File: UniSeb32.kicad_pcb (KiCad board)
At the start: 4 copper layers, 72 x 100 mm, 60 parts, among them J1 IO, J2 ARJM11C7-114-BA-EW2, J3 Conn_02x05_Odd_Even, J6 SDS011, J7 Conn_01x02_Female, J8 Conn_01x02_Female, U1 mini_esp32, U2 LAN8720A, U3 AMS1117-3.3, U4 AMS5919, U5 module_bme280, U6 RT9400, U7 MCP23008-xSS, U8 HLK-PM01, X1 233-508, X2 233-503, X3 233-504, Y1 Crystal_GND23

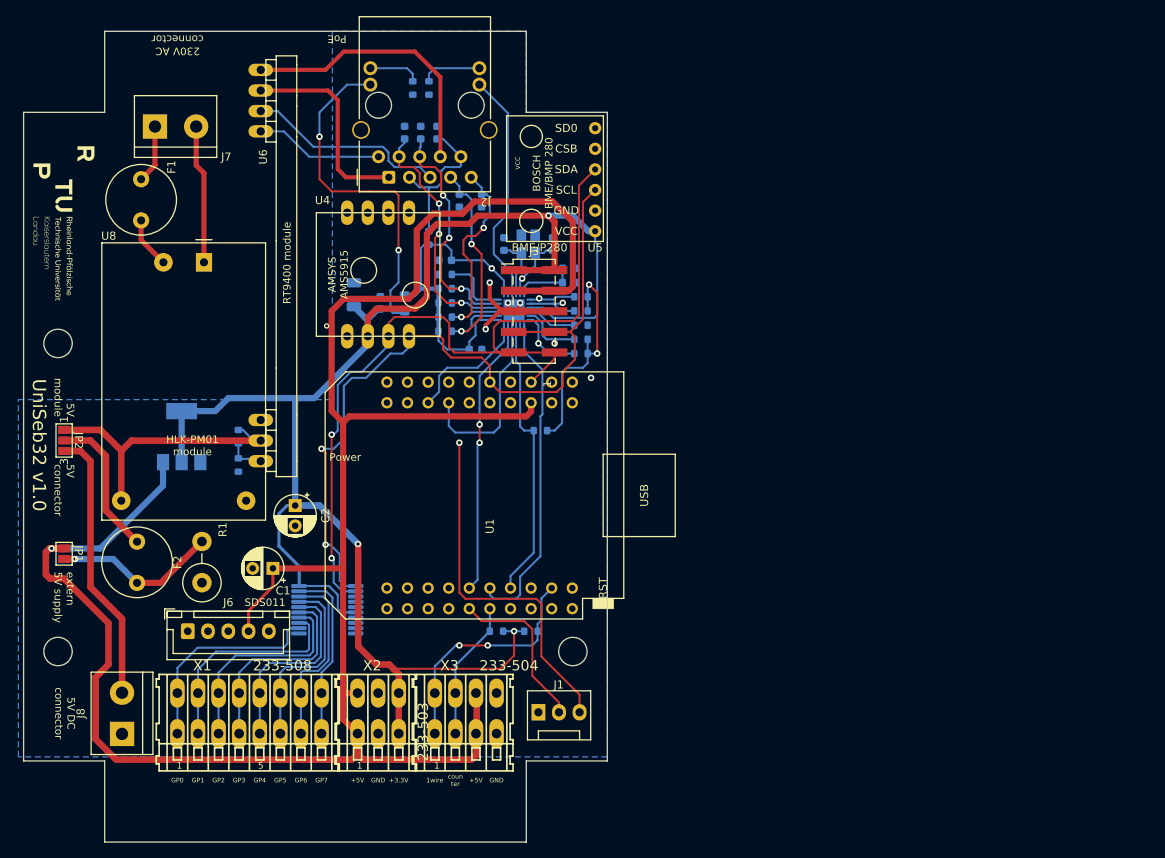
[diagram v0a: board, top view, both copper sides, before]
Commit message: Added attributes for jlcpcb assembly
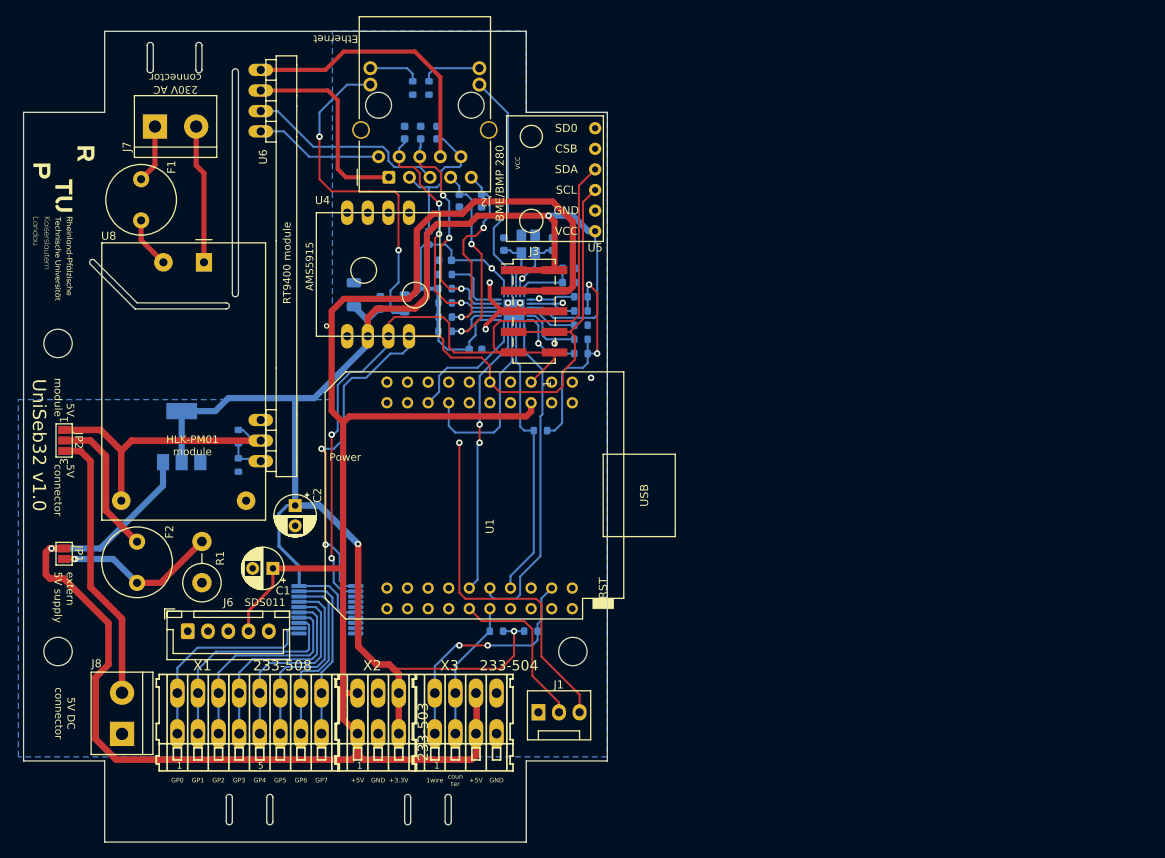
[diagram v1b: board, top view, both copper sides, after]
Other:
- outline, holes or cut-outs redrawn
- board text added: "AMS5915"
- board text added: "Ethernet"
- board text removed: "AMSYS AMS5915"
- board text removed: "BOSCH BME/BMP 280"
- board text removed: "PoE"

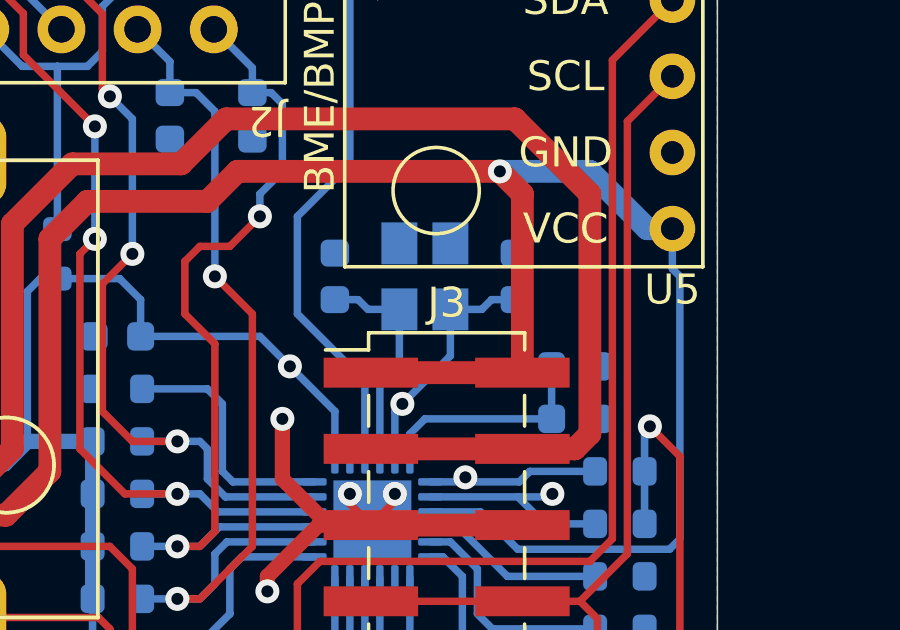
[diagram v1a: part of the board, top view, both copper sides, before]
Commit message: Fixes wrong pin numbering at Y1
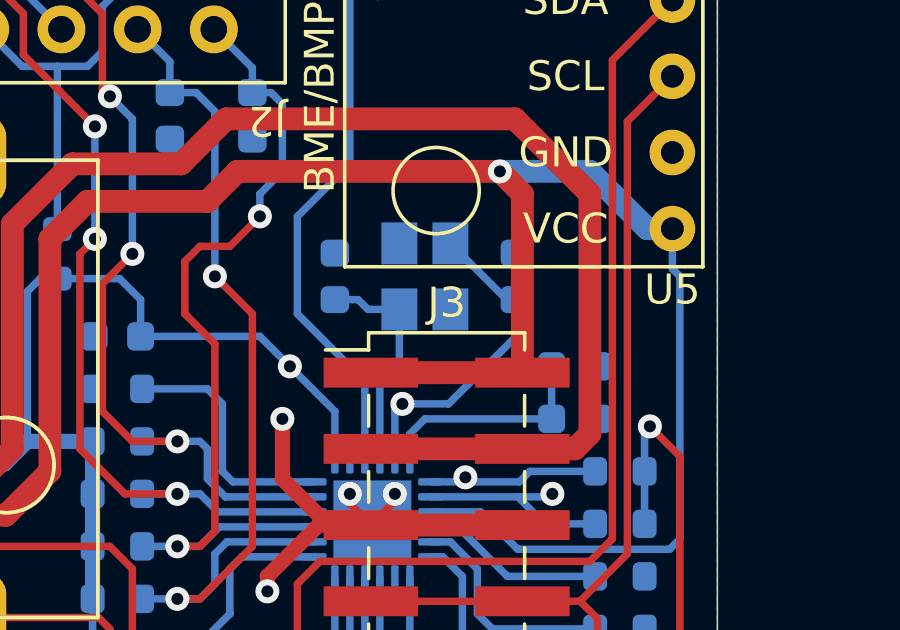
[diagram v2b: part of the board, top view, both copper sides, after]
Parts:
- Y1: value Crystal_GND23 -> 25 MHz
- turned Y1 to -90 degrees
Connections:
- Y1 pad 1: Net-(C14-Pad1) -> /IO17_RCLK
- Y1 pad 3: GND -> Net-(C14-Pad1)
- Y1 pad 4: /IO17_RCLK -> GND
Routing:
- net /IO17_RCLK: track 26.1 -> 28.9 mm

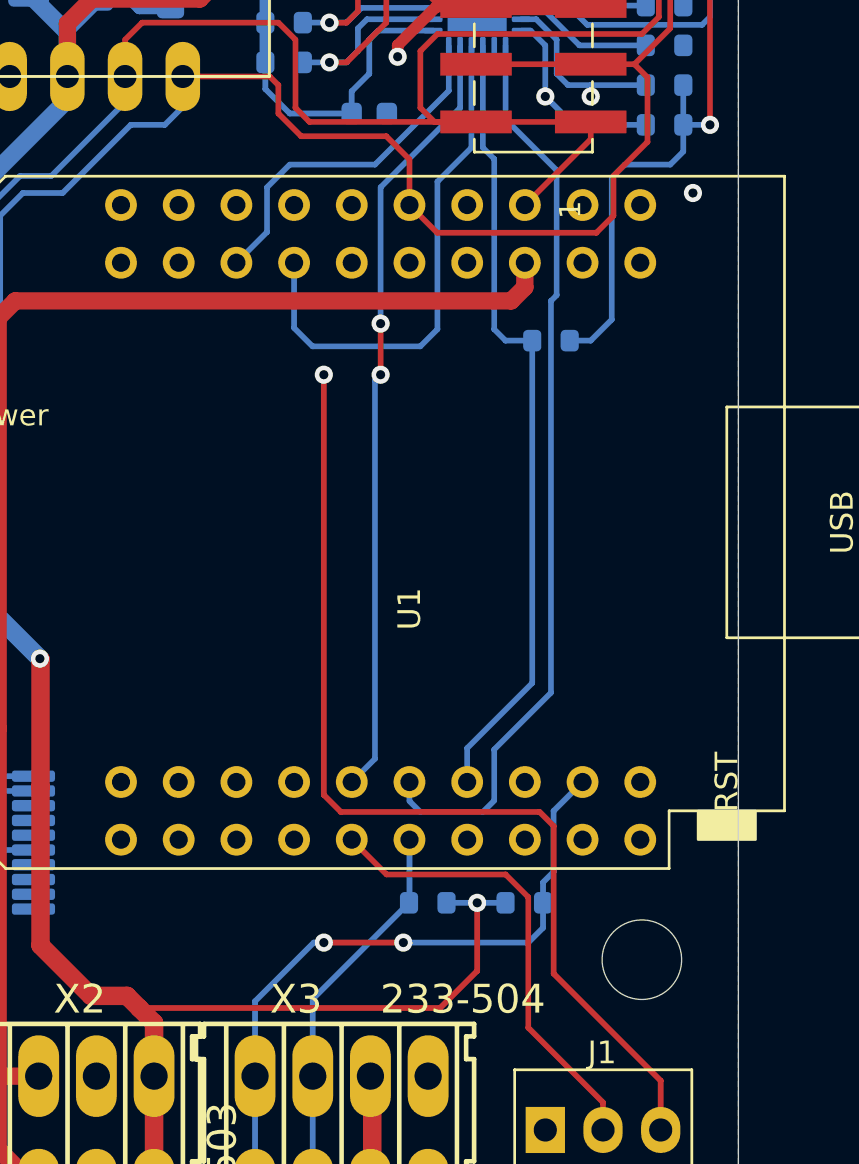
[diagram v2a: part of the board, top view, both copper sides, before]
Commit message: corrected mapping of pins added SD slot removed crystal y1 and capacitors in bom and cpl file
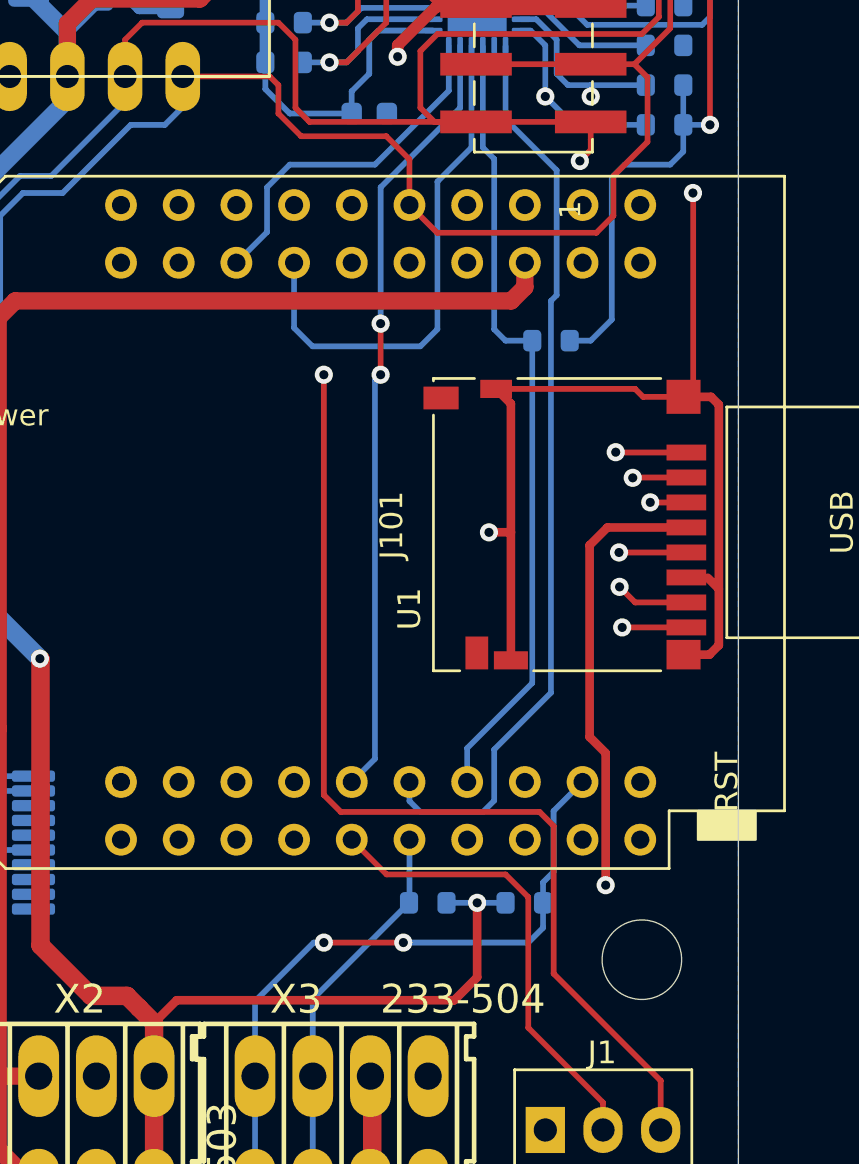
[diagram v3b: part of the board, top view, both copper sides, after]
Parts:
- added J101: Micro_SD_Card_Det, Connector_Card:microSD_HC_Hirose_DM3D-SF, F.Cu at (176.9, 112.3)
- U4: value AMS5919 -> AMS5915
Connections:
- U1 pad 13: /SDS_RX -> /SDS_TX
- U1 pad 17: unconnected-(U1-Pad17) -> /SD2
- U1 pad 19: unconnected-(U1-Pad19) -> /SCMD
- U1 pad 20: unconnected-(U1-Pad20) -> /SD3
- U1 pad 30: /SDS_TX -> /SDS_RX
- U1 pad 31: unconnected-(U1-Pad31) -> /SDA
- U1 pad 36: /SDA -> unconnected-(U1-Pad36)
- U1 pad 38: unconnected-(U1-Pad38) -> /SD1
- U1 pad 39: unconnected-(U1-Pad39) -> /SD0
- U1 pad 40: unconnected-(U1-Pad40) -> /SCLK
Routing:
- net GND: track 36.4 -> 81.9 mm, vias 5 -> 6
- net +3.3V: track 249.0 -> 274.8 mm, vias 5 -> 6
- net /SD1: track 0.00 -> 24.0 mm, vias 0 -> 1
- net /SD2: track 0.00 -> 21.7 mm, vias 0 -> 1
- net /SCLK: track 0.00 -> 20.9 mm, vias 0 -> 1
- net /SD0: track 0.00 -> 19.5 mm, vias 0 -> 1
- net /SCMD: track 0.00 -> 17.5 mm, vias 0 -> 1
- net /SD3: track 0.00 -> 16.6 mm, vias 0 -> 1
- net /SDS_RX: track 41.6 -> 53.0 mm
- net /SDS_TX: track 54.6 -> 43.8 mm
- net /SDA: track 103.5 -> 111.3 mm, vias 2 -> 3

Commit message: .
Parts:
- removed R2: 0, Resistor_SMD:R_0603_1608Metric
- moved C9 34.6 mm to (158.6, 117.3), turned to -90 degrees
- moved C13 29.0 mm to (171.5, 113.3), turned to 0 degrees
- moved C14 26.7 mm to (160.8, 105.7)
- moved C15 26.7 mm to (166.8, 105.7)
- moved Y1 26.7 mm to (163.8, 105.7)
- moved R15 25.7 mm to (171.5, 115.0)
- moved R17 25.7 mm to (171.5, 118.5)
- moved R18 25.7 mm to (171.5, 116.8)
- moved U2 25.3 mm to (163.6, 112.8)
- moved R10 25.3 mm to (155.1, 115.5)
- moved R11 25.3 mm to (155.1, 110.2)
- moved R13 25.3 mm to (155.1, 112.0)
- moved R9 25.3 mm to (155.1, 113.7)
- moved C10 24.4 mm to (160.5, 117.3), turned to -90 degrees
- moved R19 24.0 mm to (171.5, 109.7)
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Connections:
- C4 pad 2: Net-(C4-Pad2) -> 3V3-2
- J1 pad 2: /IO33 -> /IO35
- J1 pad 3: /IO32 -> /IO33
- J2 pad 4: Net-(C4-Pad2) -> 3V3-2
- J2 pad 9: Net-(C4-Pad2) -> 3V3-2
- U1 pad 28: /IO32 -> unconnected-(U1-Pad28)
- U1 pad 7: unconnected-(U1-Pad7) -> /IO35
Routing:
- net /EMAC_RXD1: track 59.0 -> 0.00 mm, vias 1 -> 0
- net GND: track 81.9 -> 24.5 mm, vias 6 -> 8
- net /IO32: track 52.5 -> 0.00 mm, vias 1 -> 0
- net /EMAC_MDI0: track 49.7 -> 0.00 mm, vias 1 -> 0
- net 3V3-2: track 82.7 -> 40.9 mm, vias 3 -> 0
- net /EMAC_MDC: track 40.3 -> 0.00 mm
- net /EMAC_RXD0: track 37.2 -> 0.00 mm, vias 1 -> 0
- net /IO5_RST: track 35.2 -> 0.00 mm
- net /EMAC_TXD0: track 34.4 -> 0.00 mm, vias 2 -> 0
- net Net-(C6-Pad1): track 29.7 -> 0.00 mm, vias 2 -> 0
- net Net-(C8-Pad1): track 32.1 -> 2.48 mm, vias 3 -> 0
- net /IO17_RCLK: track 28.9 -> 0.00 mm, vias 1 -> 0
- net /EMAC_CRS_DV: track 28.9 -> 0.00 mm, vias 1 -> 0
- net Net-(C7-Pad2): track 30.3 -> 2.25 mm, vias 3 -> 0
- net Net-(C5-Pad1): track 27.9 -> 0.00 mm, vias 2 -> 0
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- added copper zone on F.Cu, net GND

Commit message: .
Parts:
- removed C15: 30p, Capacitor_SMD:C_0603_1608Metric
- removed REF** (x3): MountingHole_3.5mm, MountingHole:MountingHole_3.5mm
- removed Y1: 25 MHz, Crystal:Crystal_SMD_3225-4Pin_3.2x2.5mm
- added JP3: SolderJumper_2_Open, Jumper:SolderJumper-2_P1.3mm_Open_Pad1.0x1.5mm, B.Cu at (148.0, 102.8)
- C14: value 30p -> 1n
- C9: value 10uf -> 10u
- moved U4 80.6 mm to (223.2, 129.8)
- moved U5 80.6 mm to (244.9, 112.0)
- moved J3 80.6 mm to (242.5, 134.3)
- moved C14 39.1 mm to (172.2, 68.2), turned to -90 degrees
- moved C3 17.6 mm to (151.2, 105.0), turned to -90 degrees
- moved L1 16.9 mm to (154.5, 104.8)
- moved R11 16.2 mm to (157.5, 94.2), turned to -90 degrees
- moved R9 15.7 mm to (155.5, 98.0), turned to -90 degrees
- moved R16 15.7 mm to (165.5, 103.2)
- moved C10 14.8 mm to (160.2, 102.5)
- moved C9 14.8 mm to (158.3, 102.5)
- moved C13 14.8 mm to (171.8, 98.5)
- moved J101 14.8 mm to (177.1, 97.6)
- moved R15 14.8 mm to (171.8, 100.3)
- moved R17 14.8 mm to (171.8, 103.8)
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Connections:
- C14 pad 1: Net-(C14-Pad1) -> Net-(J2-PadSH)
- J2 pad 11: +3.3V -> 3V3-2
- J2 pad SH: GND -> Net-(J2-PadSH)
- U2 pad 4: Net-(C14-Pad1) -> unconnected-(U2-Pad4)
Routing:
- net +3.3V: track 249.1 -> 132.6 mm, vias 6 -> 3
- net +5V: track 263.4 -> 149.9 mm
- net /SDA: track 111.3 -> 6.26 mm, vias 2 -> 1
- net /SCL: track 98.2 -> 7.73 mm, vias 2 -> 1
- net Net-(C6-Pad1): track 0.00 -> 61.2 mm, vias 0 -> 2
- net Net-(C5-Pad1): track 0.00 -> 58.3 mm, vias 0 -> 2
- net Net-(C7-Pad2): track 2.25 -> 56.0 mm
- net Net-(C8-Pad1): track 2.48 -> 56.3 mm
- net /EMAC_CRS_DV: track 0.00 -> 28.9 mm, vias 0 -> 1
- net /EMAC_RXD0: track 0.00 -> 27.8 mm, vias 0 -> 1
- net /SDS_RX: track 60.1 -> 35.8 mm
- net /EMAC_TX_EN: track 0.00 -> 24.2 mm, vias 0 -> 1
- net /EMAC_RXD1: track 0.00 -> 24.1 mm, vias 0 -> 1
- net GND: track 24.5 -> 0.62 mm, vias 8 -> 6
- net Net-(J2-Pad13): track 19.8 -> 42.1 mm
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
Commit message: .
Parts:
- added C15: 1n, Capacitor_SMD:C_0603_1608Metric, B.Cu at (171.0, 64.2)
- moved J3 94.6 mm to (148.2, 126.5)
- moved U5 67.4 mm to (177.7, 115.5)
- moved U4 62.3 mm to (161.2, 123.2)
- moved C14 19.7 mm to (153.0, 64.2), turned to 90 degrees
- moved C6 8.25 mm to (164.0, 67.5), turned to 90 degrees
- moved C5 7.27 mm to (167.5, 67.5), turned to 90 degrees
- moved C4 5.03 mm to (165.8, 67.5), turned to -90 degrees
- moved C1 3.12 mm to (141.4, 118.8)
- moved J6 2.02 mm to (130.8, 128.7)
- moved U6 1.30 mm to (143.8, 82.5)
- moved C3 1.25 mm to (151.2, 103.8)
- moved R1 0.87 mm to (134.0, 122.3)
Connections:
- net Net-(C5-Pad1) renamed /TX_P
- net Net-(C6-Pad1) renamed /TX_N
- net Net-(C7-Pad2) renamed /RX_P
- net Net-(C8-Pad1) renamed /RX_N
- C14 pad 1: Net-(J2-PadSH) -> Net-(J2-PadSH2)
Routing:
- net 3V3-2: track 32.3 -> 122.3 mm, vias 0 -> 8
- net /SDS_TX: track 41.3 -> 0.00 mm
- net /SDS_RX: track 35.8 -> 0.00 mm
- net +3.3V: track 132.6 -> 167.4 mm, vias 3 -> 5
- net +5V: track 149.9 -> 116.9 mm
- net /EMAC_TXD0: track 12.9 -> 24.3 mm
- net /EMAC_MDI0: track 7.26 -> 17.7 mm, vias 0 -> 1
- net /RX_P: track 56.0 -> 45.9 mm, vias 0 -> 2
- net /RX_N: track 56.3 -> 46.5 mm, vias 0 -> 2
- net /EMAC_RXD1: track 24.1 -> 28.2 mm
- net /SD2: track 18.0 -> 21.7 mm, vias 0 -> 1
- net Net-(J2-Pad13): track 42.1 -> 45.5 mm, vias 0 -> 1
- net Net-(J2-PadSH2): track 0.00 -> 2.62 mm
- net Net-(J2-PadSH1): track 0.00 -> 2.62 mm
- net /SCMD: track 15.4 -> 17.5 mm
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- added copper zone on In1.Cu, net GND
- added copper zone on In2.Cu, net GND
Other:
- outline, holes or cut-outs redrawn

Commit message: .
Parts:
- moved C4 10.3 mm to (173.4, 74.4), turned to 180 degrees
- moved J6 1.77 mm to (129.0, 128.8)
- moved R7 1.74 mm to (137.4, 105.7)
- moved R6 1.62 mm to (137.4, 108.8)
- moved C6 1.61 mm to (165.6, 67.5)
- moved R8 1.33 mm to (163.8, 62.0)
- moved C1 1.06 mm to (140.5, 118.2)
- moved R1 0.18 mm to (133.9, 122.4)
- moved C5 0.11 mm to (167.4, 67.5)
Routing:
- net +5V: track 116.9 -> 234.8 mm, vias 1 -> 3
- net /SCL: track 7.73 -> 121.3 mm, vias 1 -> 3
- net /SDA: track 6.26 -> 117.4 mm, vias 1 -> 2
- net /SDS_RX: track 0.00 -> 71.3 mm
- net /SDS_TX: track 0.00 -> 56.1 mm
- net 3V3-2: track 122.3 -> 80.8 mm, vias 8 -> 9
- net /COUNTER: track 14.4 -> 50.8 mm
- net /IO35: track 0.00 -> 33.1 mm, vias 0 -> 1
- net /IO33: track 0.00 -> 33.1 mm, vias 0 -> 1
- net +3.3V: track 167.4 -> 189.0 mm, vias 5 -> 6
- net /ONEWIRE: track 24.3 -> 44.3 mm
- net Net-(J2-Pad14): track 7.44 -> 6.08 mm
- net GND: track 0.62 -> 0.00 mm, vias 6 -> 20
- net /EMAC_RXD0: track 27.8 -> 27.2 mm
- added copper zone on In2.Cu, net 3V3-2
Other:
- board text removed: "VCC"
